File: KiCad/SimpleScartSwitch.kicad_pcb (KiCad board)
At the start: 2 copper layers, 61 x 86.4 mm, 8 parts, among them CN1 SCART-F, CN2 SCART-F, J1 Conn_02x04_Odd_Even, SW1 SW_8PDT

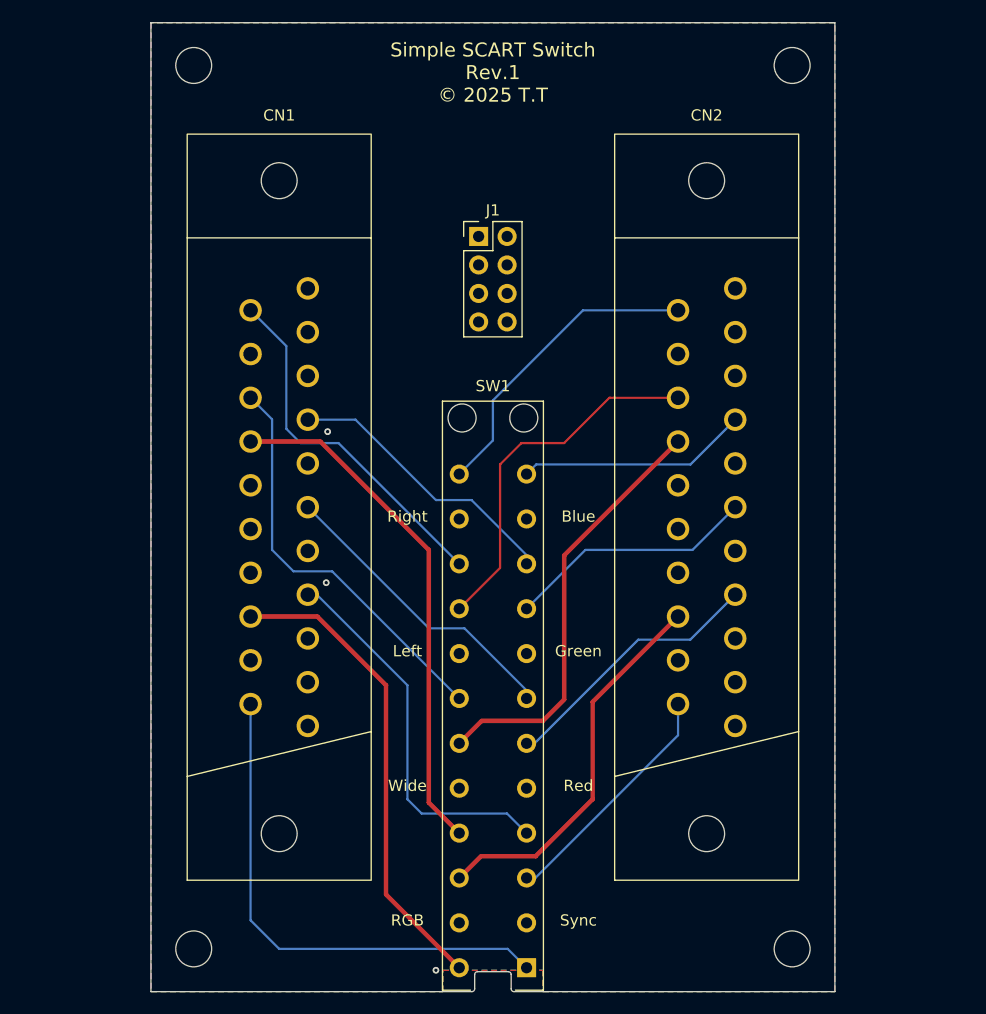
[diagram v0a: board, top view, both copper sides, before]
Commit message: SCART plugs can be soldered directly to the board
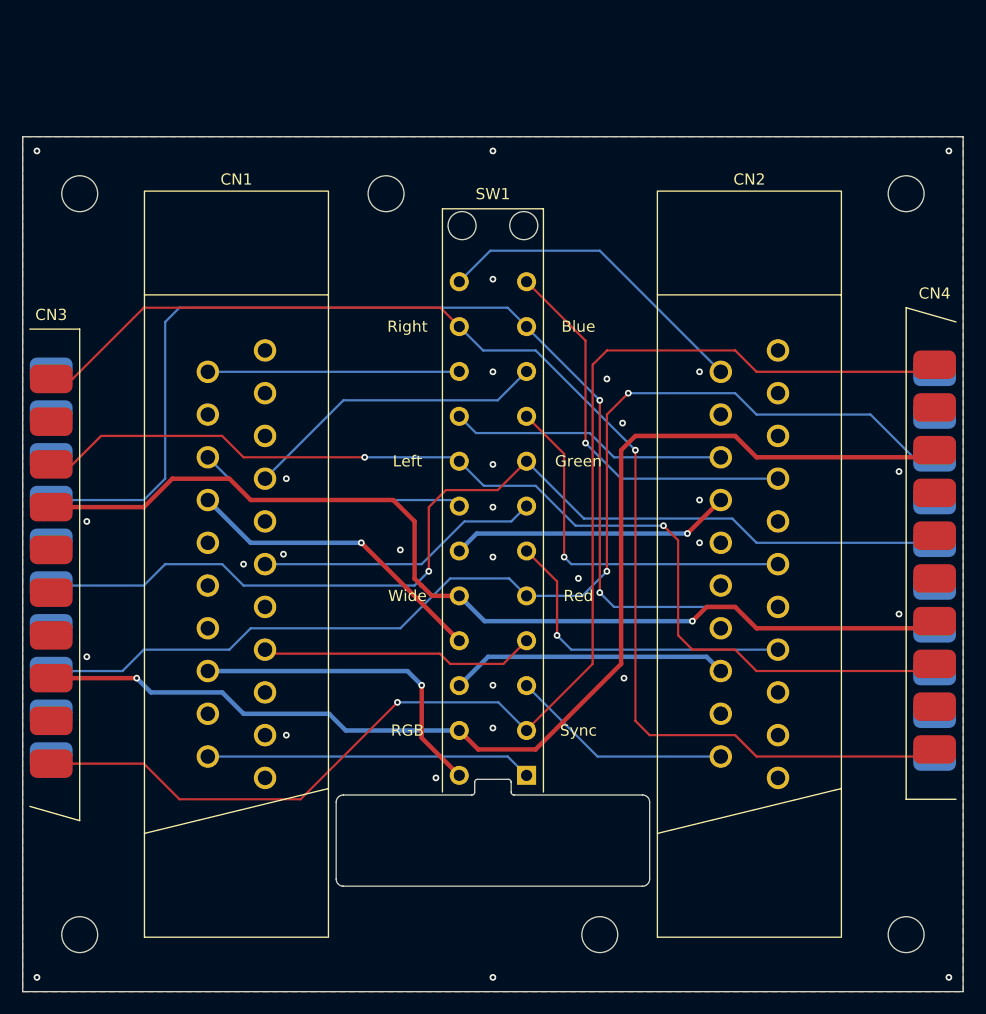
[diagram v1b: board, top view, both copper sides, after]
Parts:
- removed J1: Conn_02x04_Odd_Even, Connector_PinHeader_2.54mm:PinHeader_2x04_P2.54mm_Vertical
- removed the REF** at (109.2, 134.6)
- removed the REF** at (162.6, 134.6)
- added CN3: Conn_02x10_Odd_Even, Library:SCART_Plug, F.Cu at (96.5, 100.3)
- added CN4: Conn_02x10_Odd_Even, Library:SCART_Plug, F.Cu at (175.3, 100.3)
- added REF**: MountingHole_3.2mm_M3, MountingHole:MountingHole_3.2mm_M3, F.Cu at (126.4, 67.3)
- added REF**: MountingHole_3.2mm_M3, MountingHole:MountingHole_3.2mm_M3, F.Cu at (172.7, 133.3)
- added REF**: MountingHole_3.2mm_M3, MountingHole:MountingHole_3.2mm_M3, F.Cu at (99.1, 133.3)
- added REF**: MountingHole_3.2mm_M3, MountingHole:MountingHole_3.2mm_M3, F.Cu at (145.4, 133.3)
- CN1, CN2: footprint Library:SCART -> Library:SCART_Socket
- moved SW1 17.1 mm to (135.9, 97.2)
- moved REF** 15.3 mm to (172.7, 67.3)
- moved REF** 15.3 mm to (99.1, 67.3)
- moved CN1 6.35 mm to (113.0, 100.3)
- moved CN2 6.35 mm to (158.8, 100.3)
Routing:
- net Blue: track 0.00 -> 115.9 mm, vias 0 -> 2
- net Sync: track 0.00 -> 115.4 mm, vias 0 -> 1
- net Right: track 0.00 -> 112.3 mm, vias 0 -> 1
- net RGB: track 0.00 -> 105.2 mm, vias 0 -> 1
- net Red: track 0.00 -> 100.8 mm, vias 0 -> 2
- net Left: track 0.00 -> 93.7 mm, vias 0 -> 2
- net Green: track 0.00 -> 91.3 mm, vias 0 -> 1
- net Wide: track 0.00 -> 89.6 mm, vias 0 -> 1
- net Wide1: track 46.3 -> 27.6 mm, vias 0 -> 1
- net Sync1: track 45.6 -> 29.1 mm
- net Blue2: track 20.6 -> 35.0 mm, vias 0 -> 1
- net RGB1: track 42.5 -> 29.0 mm, vias 0 -> 1
- net Wide2: track 38.2 -> 25.2 mm, vias 0 -> 1
- net Left1: track 36.5 -> 24.2 mm
- net Green2: track 22.3 -> 33.3 mm, vias 0 -> 1
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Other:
- board size 61 x 86.4 mm -> 83.8 x 76.2 mm
- board text added: "Simple SCART Switch Rev.2 © 2025 T.T"
- board text removed: "Simple SCART Switch Rev.1 © 2025 T.T"
